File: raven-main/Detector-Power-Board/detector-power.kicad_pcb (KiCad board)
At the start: 2 copper layers, 36 parts, among them J1 DeployLipo, J2 Conn_01x04, J9 UCLipo, Q1 SQJQ100EL, T1 Transformer_1P_1S, U6 LM5185QPWPRQ1, U7 TPS7A4701xRGW, U8 TPS7A4701xRGW

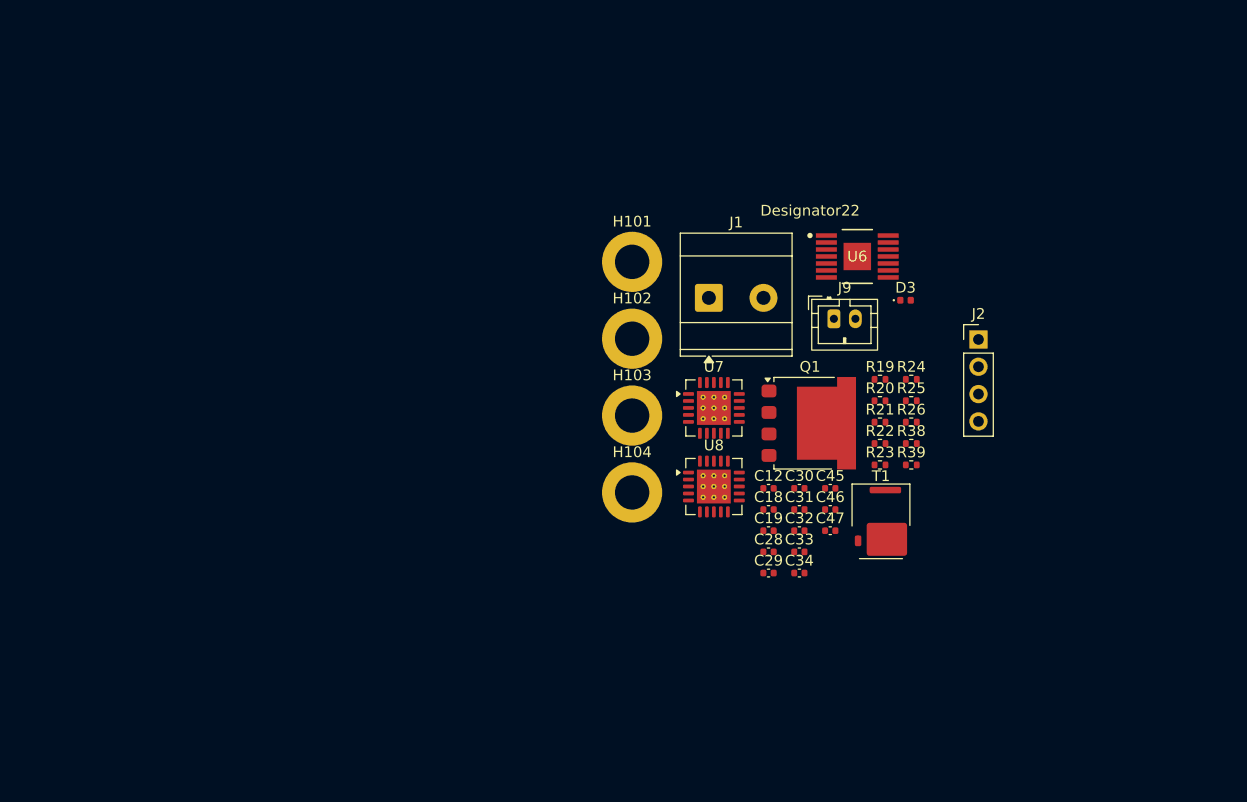
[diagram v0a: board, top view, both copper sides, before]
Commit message: Organising parts in layout
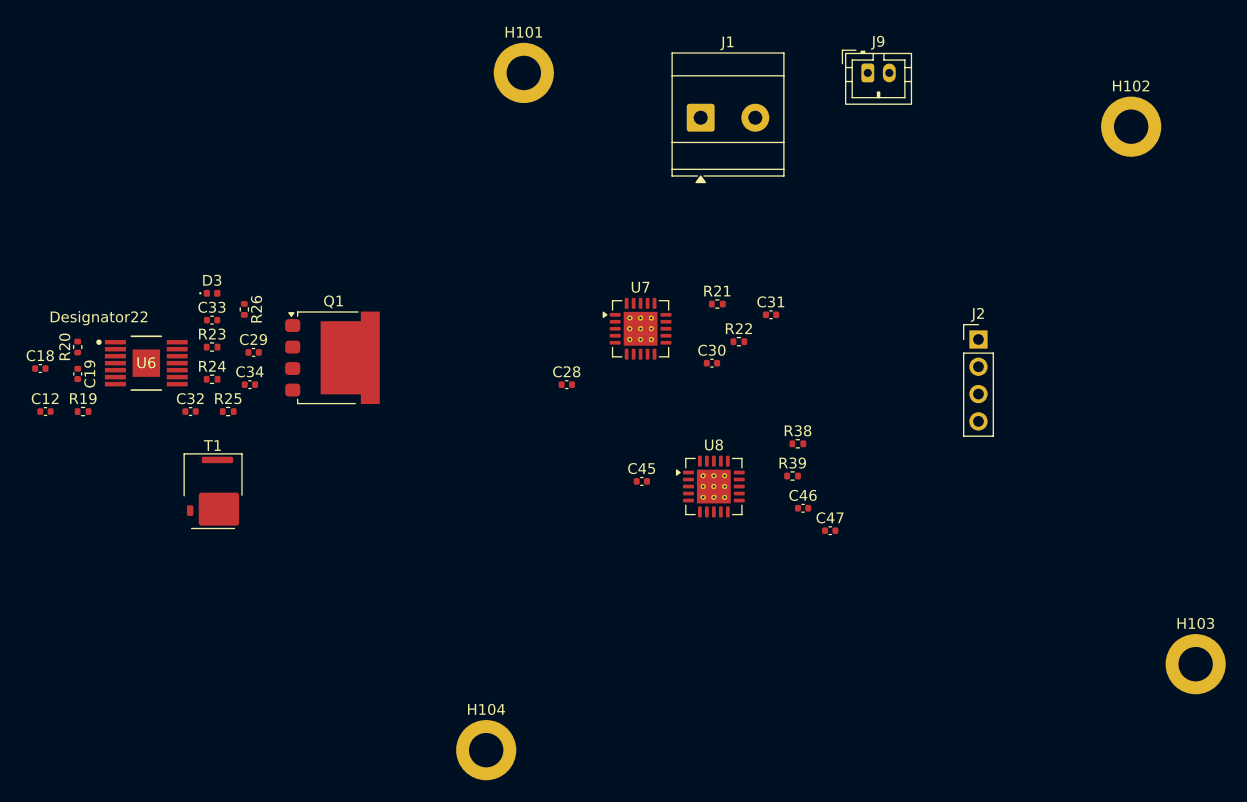
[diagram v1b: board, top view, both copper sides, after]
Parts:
- moved R20 74.8 mm to (82.5, 85.0), turned to 90 degrees
- moved R19 74.2 mm to (83.0, 91.0)
- moved C18 69.0 mm to (79.0, 87.0)
- moved C12 67.6 mm to (79.5, 91.0)
- moved U6 66.9 mm to (88.9, 86.5)
- moved C19 65.9 mm to (82.5, 87.5), turned to -90 degrees
- moved R24 65.0 mm to (95.0, 88.0)
- moved D3 64.5 mm to (95.0, 80.0)
- moved R25 63.6 mm to (96.5, 91.0)
- moved R23 63.1 mm to (95.0, 85.0)
- moved R26 62.9 mm to (98.0, 81.5), turned to -90 degrees
- moved T1 62.2 mm to (95.1, 98.4)
- moved C33 58.7 mm to (95.0, 82.5)
- moved C32 57.7 mm to (93.0, 91.0)
- moved H103 57.3 mm to (186.5, 114.5)
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
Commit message: Tidying layout a bit
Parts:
- moved C18 46.2 mm to (121.5, 68.8), turned to -90 degrees
- moved C12 43.8 mm to (117.5, 69.2), turned to -90 degrees
- moved R20 42.9 mm to (123.5, 72.2), turned to 0 degrees
- moved C19 41.4 mm to (121.0, 72.2), turned to 180 degrees
- moved R19 39.0 mm to (117.5, 72.7), turned to -90 degrees
- moved U6 34.0 mm to (122.0, 78.6), turned to -90 degrees
- moved D3 33.8 mm to (128.5, 84.7), turned to -90 degrees
- moved H103 31.8 mm to (159.0, 98.5)
- moved C33 31.1 mm to (126.0, 84.7), turned to -90 degrees
- moved R26 29.7 mm to (127.0, 87.7), turned to 180 degrees
- moved R23 28.5 mm to (123.5, 84.7), turned to -90 degrees
- moved H104 26.4 mm to (108.8, 98.8)
- moved C32 25.9 mm to (117.5, 82.7), turned to -90 degrees
- moved R24 25.7 mm to (120.5, 84.7), turned to -90 degrees
- moved C29 24.3 mm to (123.0, 88.6), turned to -90 degrees
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
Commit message: Very minor changes
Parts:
- moved H103 6.04 mm to (153.5, 96.0)
- moved H102 5.70 mm to (152.0, 69.0)
- moved H101 3.64 mm to (110.0, 70.5)
- moved J9 3.61 mm to (144.0, 71.0)
- moved C46 2.70 mm to (145.0, 96.0)
- moved C47 2.55 mm to (148.5, 96.5)
- moved J2 2.51 mm to (152.0, 81.5)
- moved R38 2.17 mm to (145.0, 90.5), turned to 180 degrees
- moved H104 1.84 mm to (110.0, 97.5)
- moved C12 1.83 mm to (119.0, 70.3)
- moved R39 1.67 mm to (145.0, 93.3)
- moved C18 1.52 mm to (121.5, 70.3)
- moved R19 1.50 mm to (119.0, 72.7)
- moved J1 1.41 mm to (131.5, 69.0)
- moved C19 0.27 mm to (121.0, 72.5)
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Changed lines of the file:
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@@
 	(footprint "Capacitor_SMD:C_0402_1005Metric"
 		(layer "F.Cu")
-		(at 150.1875 98.41)
+		(at 148.5 96.5)
 		(descr "Capacitor SMD 0402 (1005 Metric), square (rectangular) end terminal, IPC-7351 nominal, (Body size source: IPC-SM-782 page 76, https://www.pcb-3d.com/wordpress/wp-content/uploads/ipc-sm-782a_amendment_1_and_2.pdf)")
 		(tags "capacitor")
@@
 	(footprint "Resistor_SMD:R_0402_1005Metric"
 		(layer "F.Cu")
-		(at 123.5 72.23)
+		(at 123.5 72.5)
 		(descr "Resistor SMD 0402 (1005 Metric), square (rectangular) end terminal, IPC-7351 nominal, (Body size source: IPC-SM-782 page 72, https://www.pcb-3d.com/wordpress/wp-content/uploads/ipc-sm-782a_amendment_1_and_2.pdf)")
 		(tags "resistor")
@@
 	(footprint "Resistor_SMD:R_0402_1005Metric"
 		(layer "F.Cu")
-		(at 147.1725 90.325)
+		(at 145.01 90.5 180)
 		(descr "Resistor SMD 0402 (1005 Metric), square (rectangular) end terminal, IPC-7351 nominal, (Body size source: IPC-SM-782 page 72, https://www.pcb-3d.com/wordpress/wp-content/uploads/ipc-sm-782a_amendment_1_and_2.pdf)")
 		(tags "resistor")
@@
 		(duplicate_pad_numbers_are_jumpers no)
 		(fp_line
-			(start -0.153641 -0.38)
-			(end 0.153641 -0.38)
+			(start -0.153641 0.38)
+			(end 0.153641 0.38)
 			(stroke
 				(width 0.12)
@@
 		)
 		(fp_line
-			(start -0.153641 0.38)
-			(end 0.153641 0.38)
+			(start -0.153641 -0.38)
+			(end 0.153641 -0.38)
 			(stroke
 				(width 0.12)
@@
 		)
 		(pad "1" smd roundrect
-			(at -0.51 0)
+			(at -0.51 0 180)
 			(size 0.54 0.64)
 			(layers "F.Cu" "F.Mask" "F.Paste")
@@
 		)
 		(pad "2" smd roundrect
-			(at 0.51 0)
+			(at 0.51 0 180)
 			(size 0.54 0.64)
 			(layers "F.Cu" "F.Mask" "F.Paste")
@@
 	(footprint "Capacitor_SMD:C_0402_1005Metric"
 		(layer "F.Cu")
-		(at 121.5 68.75 -90)
+		(at 121.5 70.27 -90)
 		(descr "Capacitor SMD 0402 (1005 Metric), square (rectangular) end terminal, IPC-7351 nominal, (Body size source: IPC-SM-782 page 76, https://www.pcb-3d.com/wordpress/wp-content/uploads/ipc-sm-782a_amendment_1_and_2.pdf)")
 		(tags "capacitor")
@@
 	(footprint "Capacitor_SMD:C_0402_1005Metric"
 		(layer "F.Cu")
-		(at 117.5 69.23 -90)
+		(at 119 70.27 -90)
 		(descr "Capacitor SMD 0402 (1005 Metric), square (rectangular) end terminal, IPC-7351 nominal, (Body size source: IPC-SM-782 page 76, https://www.pcb-3d.com/wordpress/wp-content/uploads/ipc-sm-782a_amendment_1_and_2.pdf)")
 		(tags "capacitor")
@@
 	(footprint "Connector_JST:JST_PH_B2B-PH-K_1x02_P2.00mm_Vertical"
 		(layer "F.Cu")
-		(at 147 69)
+		(at 144 71)
 		(descr "JST PH series connector, B2B-PH-K (http://www.jst-mfg.com/product/pdf/eng/ePH.pdf)")
 		(tags "connector JST PH vertical")
@@
 	(footprint "Capacitor_SMD:C_0402_1005Metric"
 		(layer "F.Cu")
-		(at 121 72.23 180)
+		(at 121 72.5 180)
 		(descr "Capacitor SMD 0402 (1005 Metric), square (rectangular) end terminal, IPC-7351 nominal, (Body size source: IPC-SM-782 page 76, https://www.pcb-3d.com/wordpress/wp-content/uploads/ipc-sm-782a_amendment_1_and_2.pdf)")
 		(tags "capacitor")
@@
 	(footprint "Connector_PinHeader_2.54mm:PinHeader_1x04_P2.54mm_Vertical"
 		(layer "F.Cu")
-		(at 154.5 81.69)
+		(at 152 81.46)
 		(descr "Through hole straight pin header, 1x04, 2.54mm pitch, single row")
 		(tags "Through hole pin header THT 1x04 2.54mm single row")
@@
 	(footprint "MountingHole:MountingHole_3.2mm_M3_DIN965_Pad"
 		(layer "F.Cu")
-		(at 159 98.5)
+		(at 153.5 96)
 		(descr "Mounting Hole 3.2mm, M3, generated by kicad-footprint-generator mountinghole.py")
 		(tags "mountinghole M3 DIN965")
@@
 	(footprint "Resistor_SMD:R_0402_1005Metric"
 		(layer "F.Cu")
-		(at 117.5 72.73 -90)
+		(at 119 72.73 -90)
 		(descr "Resistor SMD 0402 (1005 Metric), square (rectangular) end terminal, IPC-7351 nominal, (Body size source: IPC-SM-782 page 72, https://www.pcb-3d.com/wordpress/wp-content/uploads/ipc-sm-782a_amendment_1_and_2.pdf)")
 		(tags "resistor")
@@
 		)
 		(fp_text user "${REFERENCE}"
-			(at 0 0 90)
+			(at 0.27 0 90)
 			(layer "F.Fab")
 			(effects
@@
 	(footprint "Capacitor_SMD:C_0402_1005Metric"
 		(layer "F.Cu")
-		(at 147.6625 96.325)
+		(at 144.98 96)
 		(descr "Capacitor SMD 0402 (1005 Metric), square (rectangular) end terminal, IPC-7351 nominal, (Body size source: IPC-SM-782 page 76, https://www.pcb-3d.com/wordpress/wp-content/uploads/ipc-sm-782a_amendment_1_and_2.pdf)")
 		(tags "capacitor")
@@
 	(footprint "Resistor_SMD:R_0402_1005Metric"
 		(layer "F.Cu")
-		(at 146.6825 93.325)
+		(at 145.01 93.325)
 		(descr "Resistor SMD 0402 (1005 Metric), square (rectangular) end terminal, IPC-7351 nominal, (Body size source: IPC-SM-782 page 72, https://www.pcb-3d.com/wordpress/wp-content/uploads/ipc-sm-782a_amendment_1_and_2.pdf)")
 		(tags "resistor")
@@
 	(footprint "MountingHole:MountingHole_3.2mm_M3_DIN965_Pad"
 		(layer "F.Cu")
-		(at 108.75 98.85)
+		(at 110 97.5)
 		(descr "Mounting Hole 3.2mm, M3, generated by kicad-footprint-generator mountinghole.py")
 		(tags "mountinghole M3 DIN965")
@@
 	(footprint "MountingHole:MountingHole_3.2mm_M3_DIN965_Pad"
 		(layer "F.Cu")
-		(at 157.5 70.5)
+		(at 152 69)
 		(descr "Mounting Hole 3.2mm, M3, generated by kicad-footprint-generator mountinghole.py")
 		(tags "mountinghole M3 DIN965")
@@
 	(footprint "MountingHole:MountingHole_3.2mm_M3_DIN965_Pad"
 		(layer "F.Cu")
-		(at 109 67)
+		(at 110 70.5)
 		(descr "Mounting Hole 3.2mm, M3, generated by kicad-footprint-generator mountinghole.py")
 		(tags "mountinghole M3 DIN965")
@@
 	(footprint "TerminalBlock_Phoenix:TerminalBlock_Phoenix_MKDS-3-2-5.08_1x02_P5.08mm_Horizontal"
 		(layer "F.Cu")
-		(at 131.955 67.6675)
+		(at 131.5 69)
 		(descr "Terminal Block Phoenix MKDS-3-2-5.08, 2 pins, pitch 5.08mm, size 10.2x11.2mm, drill diameter 1.3mm, pad diameter 2.6mm, http://www.farnell.com/datasheets/2138224.pdf")
 		(tags "THT Terminal Block Phoenix MKDS-3-2-5.08 pitch 5.08mm size 10.2x11.2mm drill 1.3mm pad 2.6mm")

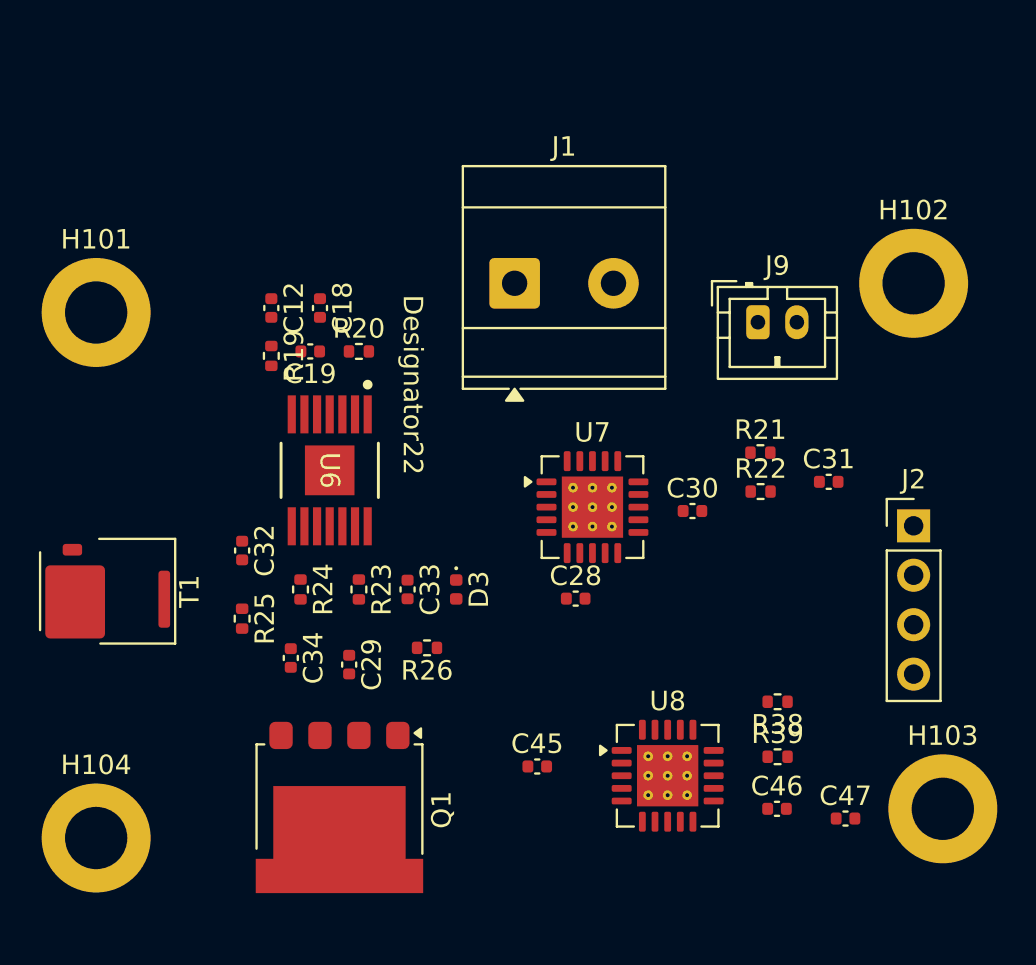
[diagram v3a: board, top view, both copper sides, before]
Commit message: Relabelled power board
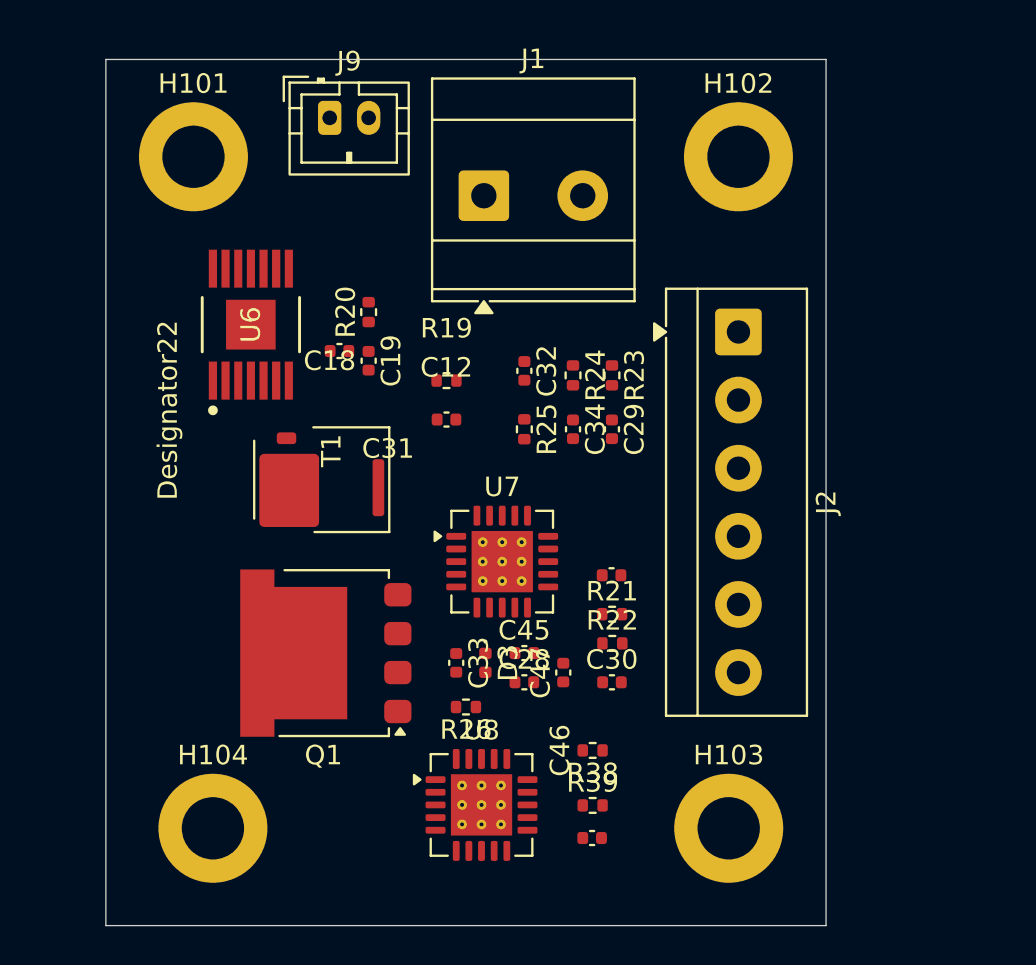
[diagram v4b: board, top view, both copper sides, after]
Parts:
- J2: value Conn_01x04 -> Conn_01x06; footprint Connector_PinHeader_2.54mm:PinHeader_1x04_P2.54mm_Vertical -> TerminalBlock_4Ucon:TerminalBlock_4Ucon_1x06_P3.50mm_Horizontal
- moved J9 24.4 mm to (122.0, 60.5)
- moved C34 18.7 mm to (134.5, 76.5)
- moved C29 18.1 mm to (136.5, 76.5)
- moved R24 17.8 mm to (134.5, 73.7)
- moved R25 17.5 mm to (132.0, 76.5)
- moved C32 17.2 mm to (132.0, 73.5)
- moved R23 17.0 mm to (136.5, 73.7)
- moved C47 16.3 mm to (134.0, 89.0), turned to 90 degrees
- moved J2 13.4 mm to (143.0, 71.5), turned to -90 degrees
- moved T1 12.4 mm to (121.6, 79.1)
- moved C31 12.1 mm to (136.5, 84.0)
- moved R21 11.3 mm to (136.5, 86.0)
- moved H102 11.1 mm to (143.0, 62.5)
- moved H103 11.0 mm to (142.5, 97.0)
- moved R22 10.9 mm to (136.5, 87.5)
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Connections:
- C12 pad 1: +50V -> GND
- C18 pad 1: +50V -> GND
- C18 pad 2: +50V -> GND
- C19 pad 1: +50V -> GND
- C28 pad 1: +50V -> GND
- C28 pad 2: +50V -> GND
- C29 pad 1: +50V -> GND
- C30 pad 2: +50V -> GND
- C31 pad 1: +5V -> /Power_Out_5V
- C31 pad 2: +50V -> GND
- C32 pad 2: +50V -> GND
- C33 pad 2: +50V -> GND
- C34 pad 1: +50V -> GND
- C34 pad 2: +50V -> GND
- C45 pad 1: +5V -> /Data_In_5V
- C45 pad 2: +50V -> GND
- C46 pad 2: +50V -> GND
- C47 pad 1: +3V3 -> /Data_Out_3V3
- C47 pad 2: +50V -> GND
- D3 pad 1: +50V -> GND
- H101 pad 1: +50V -> GND
- H102 pad 1: +50V -> GND
- H103 pad 1: +50V -> GND
- H104 pad 1: +50V -> GND
- J1 pad 1: +50V -> GND
- J1 pad 2: +50V -> GND
- J2 pad 1: +50V -> GND
- J2 pad 2: +5V -> /Power_Out_5V
- J2 pad 3: +3V3 -> /Data_In_5V
- J2 pad 4: +50V -> /Data_Out_3V3
- J9 pad 1: +50V -> GND
- J9 pad 2: +50V -> GND
- R20 pad 2: +50V -> GND
- R21 pad 1: +5V -> /Power_Out_5V
- R22 pad 2: +50V -> GND
- R25 pad 1: +50V -> GND
- R38 pad 1: +3V3 -> /Data_Out_3V3
- R39 pad 2: +50V -> GND
- T1 pad 1: +50V -> GND
- T1 pad 3: +50V -> GND
- U6 pad 1: +50V -> /ON-OFF
- U6 pad 14: +50V -> GND
- U6 pad 15: +50V -> GND
- U6 pad 5: +50V -> GND
- U6 pad 8: +50V -> GND
- U7 pad 1: +5V -> /Power_Out_5V
- U7 pad 13: +50V -> /ON-OFF
- U7 pad 15: +50V -> GND
- U7 pad 16: +50V -> GND
- U7 pad 20: +5V -> /Power_Out_5V
- U7 pad 7: +50V -> GND
- U8 pad 1: +3V3 -> /Data_Out_3V3
- U8 pad 13: +5V -> /ON-OFF
- U8 pad 15: +5V -> /Data_In_5V
- U8 pad 16: +5V -> /Data_In_5V
- U8 pad 20: +3V3 -> /Data_Out_3V3
- U8 pad 7: +50V -> GND
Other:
- board outline added: 37 x 44.5 mm

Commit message: Corrected boost
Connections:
- C18 pad 1: GND -> /BBIN
- C28 pad 1: GND -> /BBIN
- C33 pad 2: GND -> /Power_Out_50V
- C34 pad 1: GND -> /Power_Out_50V
- D3 pad 1: GND -> /Power_Out_50V
- J1 pad 1: GND -> /BBIN
- J2 pad 1: GND -> /Power_Out_50V
- J9 pad 1: GND -> /BBIN
- T1 pad 1: GND -> /BBIN
- U6 pad 14: GND -> /BBIN
- U7 pad 15: GND -> /BBIN
- U7 pad 16: GND -> /BBIN
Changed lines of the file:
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@@
 			(layers "F.Cu" "F.Mask" "F.Paste")
 			(roundrect_rratio 0.25)
-			(net "GND")
+			(net "/BBIN")
 			(pinfunction "AA_1")
 			(pintype "passive")
@@
 			(remove_unused_layers no)
 			(roundrect_rratio 0.104167)
-			(net "GND")
+			(net "/Power_Out_50V")
 			(pinfunction "Pin_1_1")
 			(pintype "passive")
@@
 			(layers "F.Cu" "F.Mask" "F.Paste")
 			(roundrect_rratio 0.25)
-			(net "GND")
+			(net "/BBIN")
 			(pintype "passive")
 		)
@@
 			(layers "F.Cu" "F.Mask" "F.Paste")
 			(roundrect_rratio 0.25)
-			(net "GND")
+			(net "/BBIN")
 			(pinfunction "IN_15")
 			(pintype "power_in")
@@
 			(layers "F.Cu" "F.Mask" "F.Paste")
 			(roundrect_rratio 0.25)
-			(net "GND")
+			(net "/BBIN")
 			(pinfunction "IN_16")
 			(pintype "passive")
@@
 			(remove_unused_layers no)
 			(roundrect_rratio 0.208333)
-			(net "GND")
+			(net "/BBIN")
 			(pinfunction "Pin_1_1")
 			(pintype "passive")
@@
 			(layers "F.Cu" "F.Mask" "F.Paste")
 			(roundrect_rratio 0.25)
-			(net "GND")
+			(net "/Power_Out_50V")
 			(pinfunction "K_1")
 			(pintype "passive")
@@
 			(size 1.955432 0.420766)
 			(layers "F.Cu" "F.Mask" "F.Paste")
-			(net "GND")
+			(net "/BBIN")
 			(pinfunction "VIN_14")
 			(pintype "power_in")
@@
 			(layers "F.Cu" "F.Mask" "F.Paste")
 			(roundrect_rratio 0.25)
-			(net "GND")
+			(net "/BBIN")
 			(pintype "passive")
 		)
@@
 			(layers "F.Cu" "F.Mask" "F.Paste")
 			(roundrect_rratio 0.25)
-			(net "GND")
+			(net "/Power_Out_50V")
 			(pintype "passive")
 		)
@@
 			(layers "F.Cu" "F.Mask" "F.Paste")
 			(roundrect_rratio 0.25)
-			(net "GND")
+			(net "/Power_Out_50V")
 			(pintype "passive")
 		)
@@
 			(remove_unused_layers no)
 			(roundrect_rratio 0.096154)
-			(net "GND")
+			(net "/BBIN")
 			(pinfunction "Pin_1_1")
 			(pintype "passive")
